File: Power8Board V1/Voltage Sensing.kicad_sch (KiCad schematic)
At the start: 13 parts, among them U14 ADS1015IDGS

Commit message: Beginning to layout.
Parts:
- removed FB5, FB6: FerriteBead, symbol Device:FerriteBead
- added FB3: FerriteBead, MPZ2012S102ATD25:BEADC2012X105N, symbol Device:FerriteBead
- C24: footprint (none) -> Capacitor_SMD:C_0805_2012Metric; Mfr. (none) -> Murata Electronics; Order Link (none) -> https://www.digikey.com/en/products/detail/murata-electroni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; Part # (none) -> GRT21BC71E106KE13L; Price (none) -> $0.32
- C25: footprint (none) -> Capacitor_SMD:C_0805_2012Metric; Mfr. (none) -> KEMET; Order Link (none) -> https://www.digikey.com/en/products/detail/kemet/C0805C104J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; Part # (none) -> C0805C104J5RACAUTO; Price (none) -> $0.109
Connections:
- net GNDA/3 is gone; now on net GND: C25.2, U14.3 (GND)
- net +3.3VA/3: now also FB3.2
- net 3.3V: now also FB3.1

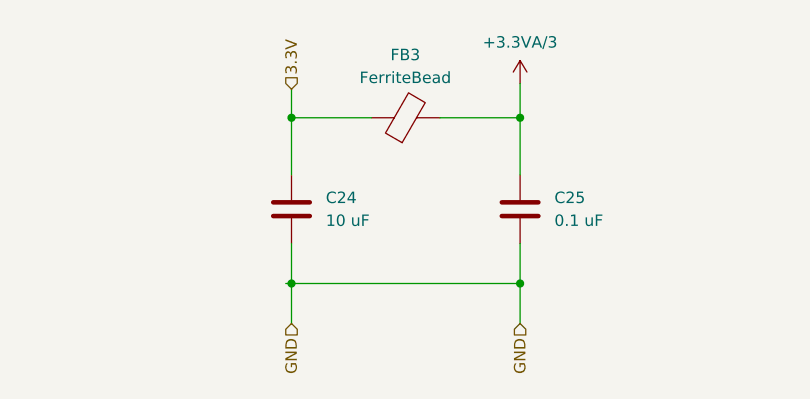
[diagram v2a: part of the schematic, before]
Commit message: Laid out components
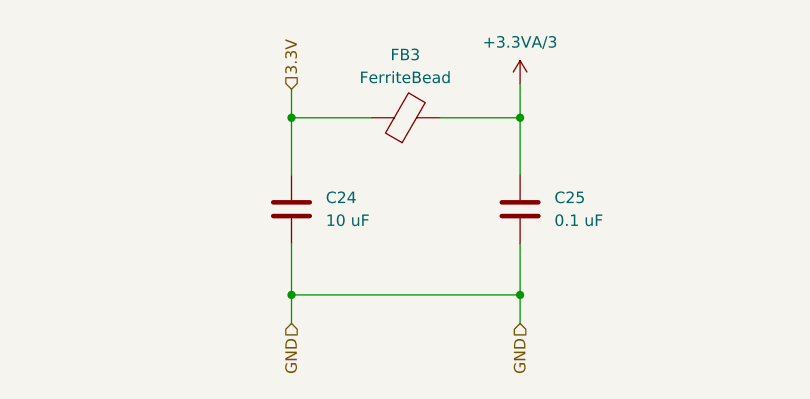
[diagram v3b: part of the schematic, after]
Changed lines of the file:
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@@
+	)
+	(junction
+		(at 60.96 169.545)
+		(diameter 0)
+		(color 0 0 0 0)
 	)
 	(junction
@@
 	)
 	(junction
-		(at 86.36 168.275)
-		(diameter 0)
-		(color 0 0 0 0)
-	)
-	(junction
 		(at 101.6 109.855)
 		(diameter 0)
@@
 	)
 	(junction
-		(at 60.96 168.275)
+		(at 86.36 169.545)
 		(diameter 0)
 		(color 0 0 0 0)
@@
 	(wire
 		(pts
+			(xy 60.96 169.545) (xy 60.96 172.72)
+		)
+		(stroke
+			(width 0)
+			(type default)
+		)
+	)
+	(wire
+		(pts
+			(xy 60.96 163.83) (xy 60.96 169.545)
+		)
+		(stroke
+			(width 0)
+			(type default)
+		)
+	)
+	(wire
+		(pts
 			(xy 97.155 109.855) (xy 101.6 109.855)
 		)
@@
 	(wire
 		(pts
+			(xy 60.96 169.545) (xy 86.36 169.545)
+		)
+		(stroke
+			(width 0)
+			(type default)
+		)
+	)
+	(wire
+		(pts
 			(xy 30.48 109.22) (xy 38.1 109.22)
 		)
@@
 	(wire
 		(pts
-			(xy 86.36 168.275) (xy 86.36 163.83)
+			(xy 86.36 163.83) (xy 86.36 169.545)
 		)
 		(stroke
@@
 	(wire
 		(pts
+			(xy 86.36 169.545) (xy 86.36 172.72)
+		)
+		(stroke
+			(width 0)
+			(type default)
+		)
+	)
+	(wire
+		(pts
 			(xy 124.46 120.015) (xy 127.635 120.015)
 		)
@@
 	(wire
 		(pts
-			(xy 60.96 168.275) (xy 60.96 172.72)
-		)
-		(stroke
-			(width 0)
-			(type default)
-		)
-	)
-	(wire
-		(pts
 			(xy 149.86 120.015) (xy 149.86 117.475)
 		)
@@
 	(wire
 		(pts
-			(xy 60.325 168.275) (xy 60.96 168.275)
-		)
-		(stroke
-			(width 0)
-			(type default)
-		)
-	)
-	(wire
-		(pts
-			(xy 60.96 163.83) (xy 60.96 168.275)
-		)
-		(stroke
-			(width 0)
-			(type default)
-		)
-	)
-	(wire
-		(pts
 			(xy 38.1 109.22) (xy 38.1 110.49)
 		)
@@
 	(wire
 		(pts
-			(xy 60.96 168.275) (xy 86.36 168.275)
-		)
-		(stroke
-			(width 0)
-			(type default)
-		)
-	)
-	(wire
-		(pts
 			(xy 124.46 114.935) (xy 127.635 114.935)
 		)
@@
 		)
 		(stroke
-			(width 0)
-			(type default)
-		)
-	)
-	(wire
-		(pts
-			(xy 86.36 168.275) (xy 86.36 172.72)
-		)
-		(stroke

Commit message: Includes most recent BOM.
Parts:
- U14: Mfr. (none) -> Texas Instruments; Order Link (none) -> https://www.digikey.com/en/products/detail/texas-instrument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; Part # (none) -> ADS1015IDGSR; Price (none) -> $2.98
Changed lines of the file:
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@@
+	)
+	(symbol
+		(lib_id "Analog_ADC:ADS1015IDGS")
+		(at 137.795 114.935 0)
+		(unit 1)
+		(exclude_from_sim no)
+		(in_bom yes)
+		(on_board yes)
+		(dnp no)
+		(fields_autoplaced yes)
+		(property "Reference" "U14"
+			(at 139.9891 99.695 0)
+			(effects
+				(font
+					(size 1.27 1.27)
+				)
+				(justify left)
+			)
+		)
+		(property "Value" "ADS1015IDGS"
+			(at 139.9891 102.235 0)
+			(effects
+				(font
+					(size 1.27 1.27)
+				)
+				(justify left)
+			)
+		)
+		(property "Footprint" "Package_SO:TSSOP-10_3x3mm_P0.5mm"
+			(at 137.795 127.635 0)
+			(effects
+				(font
+					(size 1.27 1.27)
+				)
+				(hide yes)
+			)
+		)
+		(property "Datasheet" "http://www.ti.com/lit/ds/symlink/ads1015.pdf"
+			(at 136.525 137.795 0)
+			(effects
+				(font
+					(size 1.27 1.27)
+				)
+				(hide yes)
+			)
+		)
+		(property "Description" "Ultra-Small, Low-Power, I2C-Compatible, 3.3-kSPS, 12-Bit ADCs With Internal Reference, Oscillator, and Programmable Comparator, VSSOP-10"
+			(at 137.795 114.935 0)
+			(effects
+				(font
+					(size 1.27 1.27)
+				)
+				(hide yes)
+			)
+		)
+		(property "Mfr." "Texas Instruments"
+			(at 137.795 114.935 0)
+			(effects
+				(font
+					(size 1.27 1.27)
+				)
+				(hide yes)
+			)
+		)
+		(property "Part #" "ADS1015IDGSR"
+			(at 137.795 114.935 0)
+			(effects
+				(font
+					(size 1.27 1.27)
+				)
+				(hide yes)
+			)
+		)
+		(property "Price" "$2.98"
+			(at 137.795 114.935 0)
+			(effects
+				(font
+					(size 1.27 1.27)
+				)
+				(hide yes)
+			)
+		)
+		(property "Order Link" "https://www.digikey.com/en/products/detail/texas-instruments/ADS1015IDGSR/2231559"
+			(at 137.795 114.935 0)
+			(effects
+				(font
+					(size 1.27 1.27)
+				)
+				(hide yes)
+			)
+		)
+		(pin "2"
+		)
+		(pin "9"
+		)
+		(pin "7"
+		)
+		(pin "4"
+		)
+		(pin "6"
+		)
+		(pin "8"
+		)
+		(pin "1"
+		)
+		(pin "10"
+		)
+		(pin "3"
+		)
+		(pin "5"
+		)
+		(instances
+			(project "Power8Board V1"
+				(path "/835b92cb-5206-4b93-b4be-2a785f4797f4/cc543367-03ad-4bb2-8378-8dc6c533d29a"
+					(reference "U14")
+					(unit 1)
+				)
+			)
+		)
 	)
 	(symbol
@@
 					(unit 1)
 				)
-			)
-		)
-	)
-	(symbol
-		(lib_id "Analog_ADC:ADS1015IDGS")
-		(at 137.795 114.935 0)
-		(unit 1)
-		(exclude_from_sim no)
-		(in_bom yes)
-		(on_board yes)
-		(dnp no)
-		(fields_autoplaced yes)
-		(property "Reference" "U14"
-			(at 139.9891 99.695 0)
-			(effects
-				(font
-					(size 1.27 1.27)
-				)
-				(justify left)
-			)
-		)
-		(property "Value" "ADS1015IDGS"
-			(at 139.9891 102.235 0)
-			(effects
-				(font
-					(size 1.27 1.27)
-				)
-				(justify left)
-			)
-		)
-		(property "Footprint" "Package_SO:TSSOP-10_3x3mm_P0.5mm"
-			(at 137.795 127.635 0)
-			(effects
-				(font
-					(size 1.27 1.27)
-				)
-				(hide yes)
-			)
-		)
-		(property "Datasheet" "http://www.ti.com/lit/ds/symlink/ads1015.pdf"
-			(at 136.525 137.795 0)
-			(effects
-				(font
-					(size 1.27 1.27)
-				)
-				(hide yes)
-			)
-		)
-		(property "Description" "Ultra-Small, Low-Power, I2C-Compatible, 3.3-kSPS, 12-Bit ADCs With Internal Reference, Oscillator, and Programmable Comparator, VSSOP-10"
-			(at 137.795 114.935 0)
-			(effects
-				(font
-					(size 1.27 1.27)
-				)
-				(hide yes)
-			)
-		)
-		(pin "8"
-		)
-		(pin "5"
-		)
-		(pin "6"
-		)
-		(pin "2"
-		)
-		(pin "4"
-		)
-		(pin "10"
-		)
-		(pin "3"
-		)
-		(pin "7"
-		)
-		(pin "1"
-		)
-		(pin "9"
-		)
-		(instances
-			(project ""
-				(path "/835b92cb-5206-4b93-b4be-2a785f4797f4/cc543367-03ad-4bb2-8378-8dc6c533d29a"
-					(reference "U14")
-					(unit 1)
-				)

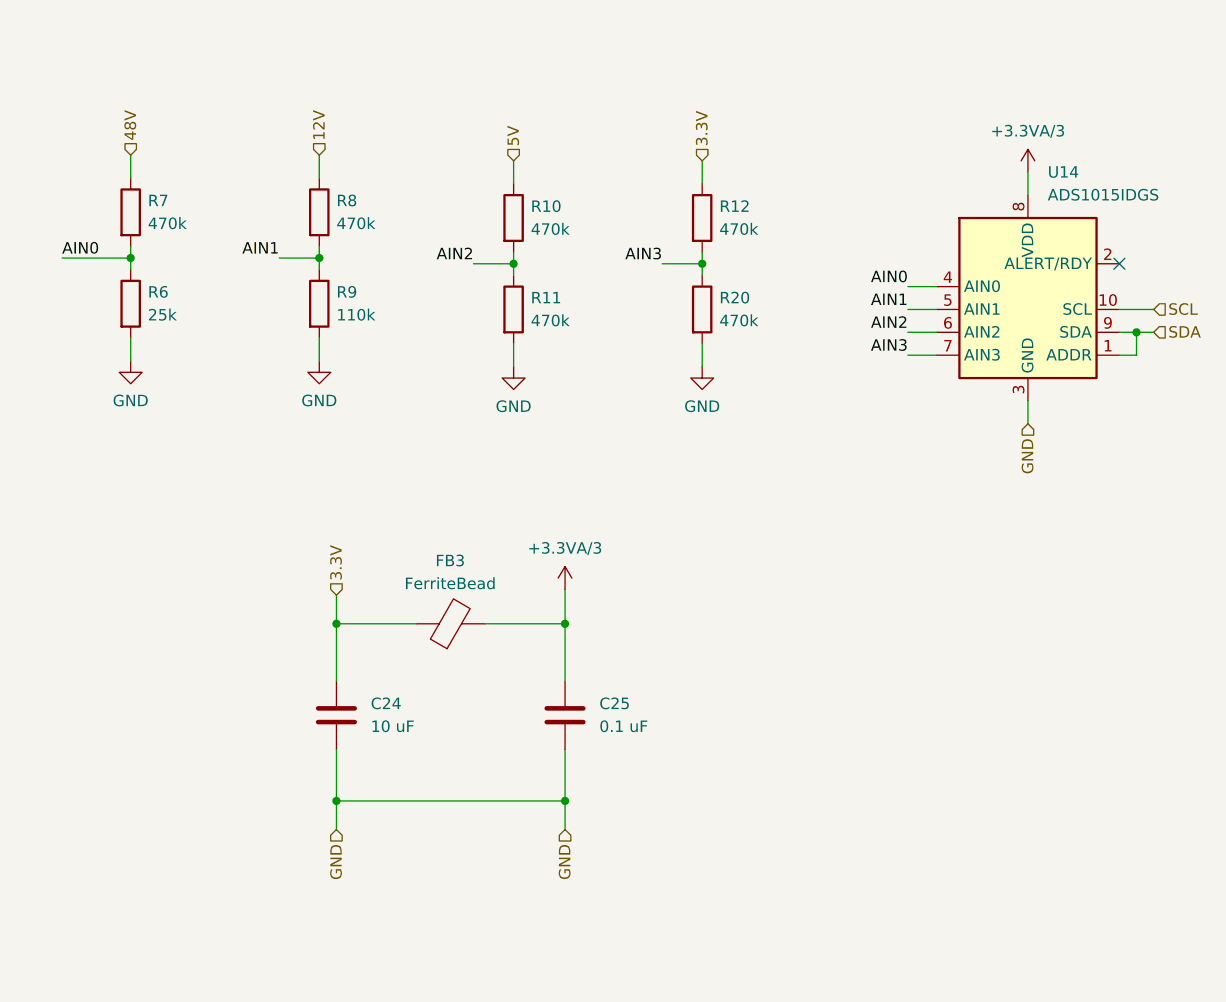
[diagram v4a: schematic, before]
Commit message: Added boxes in schematic for organization.
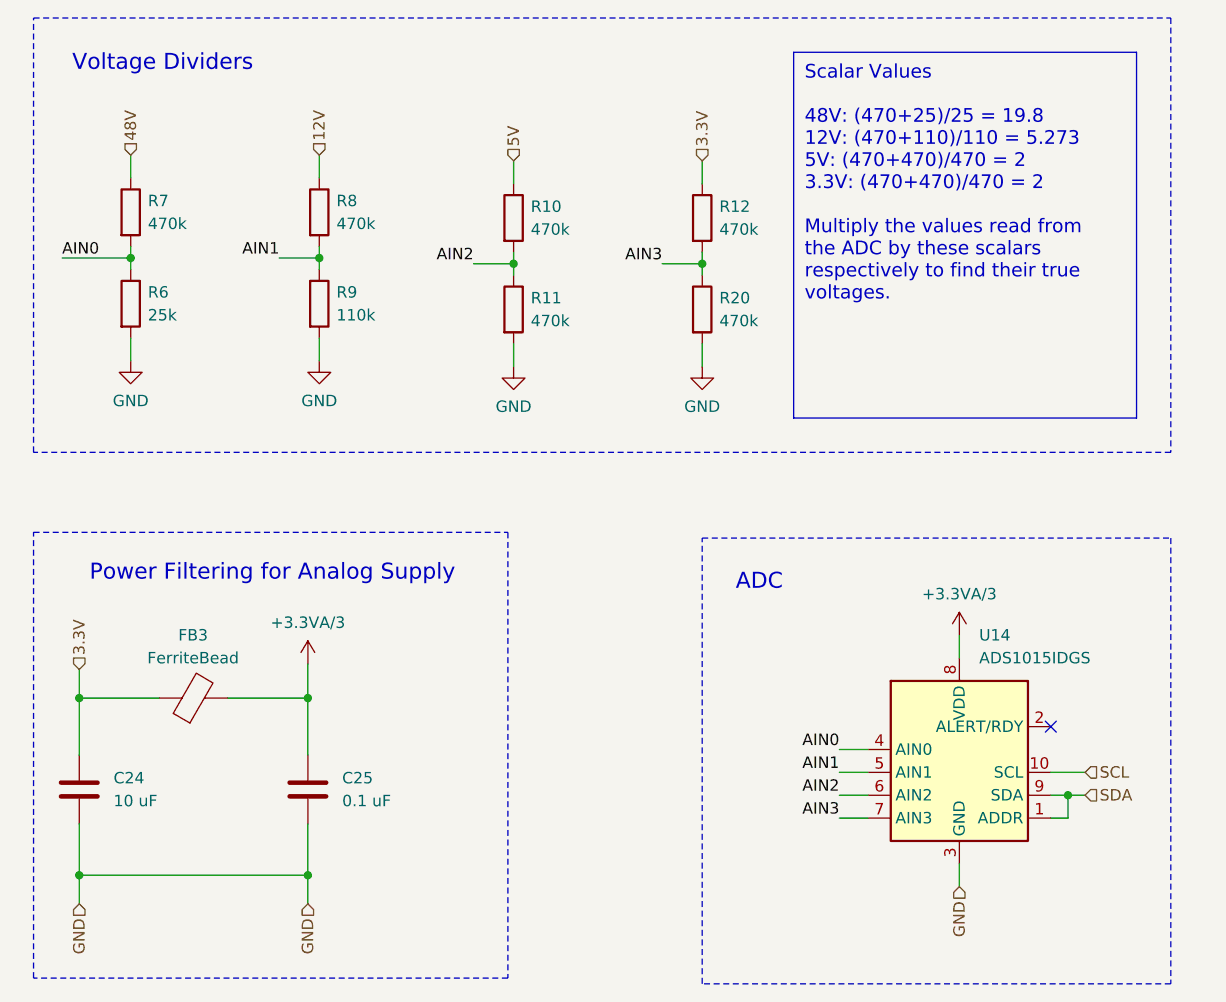
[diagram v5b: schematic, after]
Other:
- note added: "ADC"
- note added: "Power Filtering for Analog Supply"
- note added: "Voltage Dividers"
- moved on the sheet: C24, C25, FB3, U14

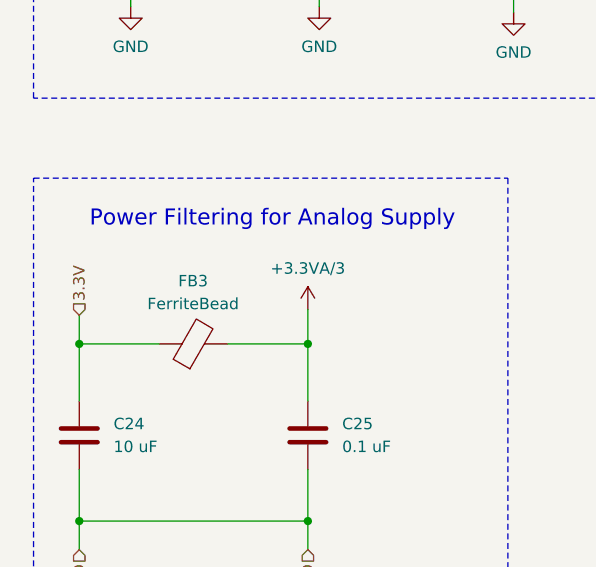
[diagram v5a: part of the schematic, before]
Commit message: Moved current sensor schematics to Current Sensor folder.
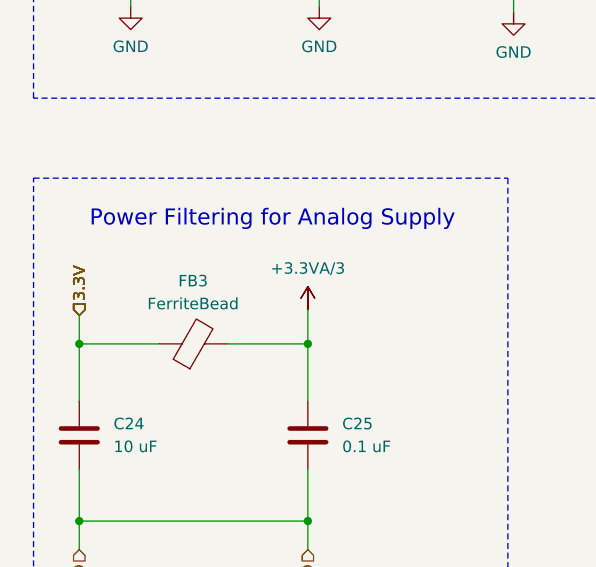
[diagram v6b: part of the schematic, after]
